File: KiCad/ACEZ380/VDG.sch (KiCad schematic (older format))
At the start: 32 parts, among them Q1 2N3904, Q100 2N3904, X1 CRYSTALHC49U-V 6.556MHz

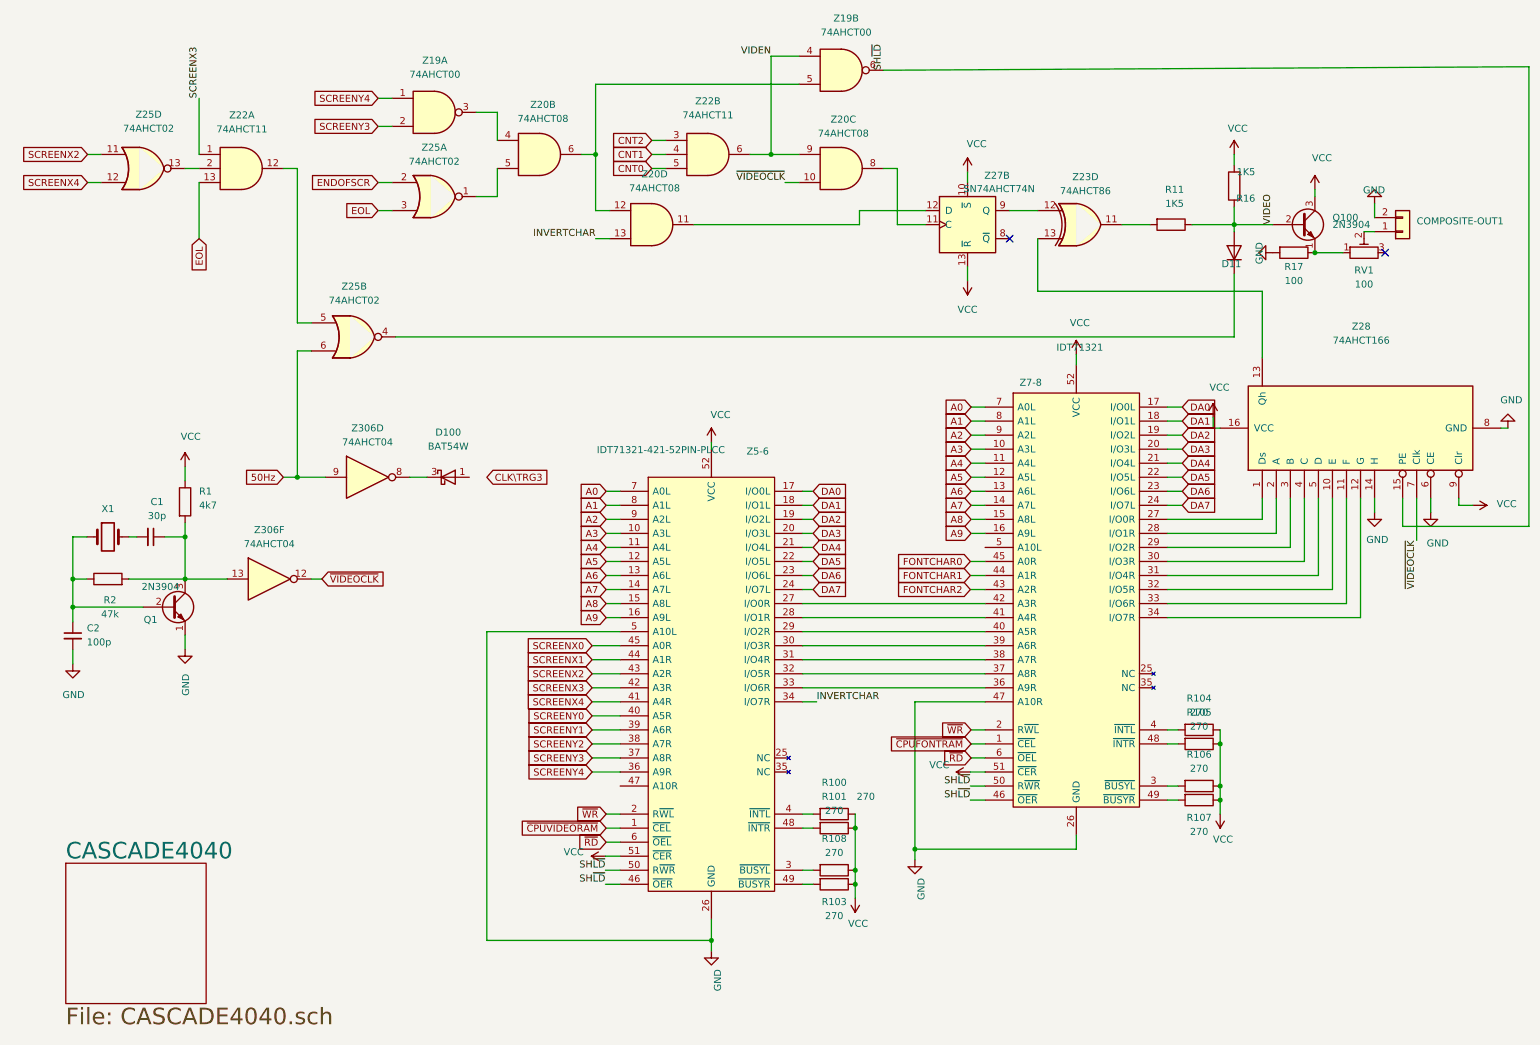
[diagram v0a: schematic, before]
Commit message: Remove SMD.
Standardise Z180 and add Z380.


Signed-off-by: John Bradley <flypie@rocketmail.com>
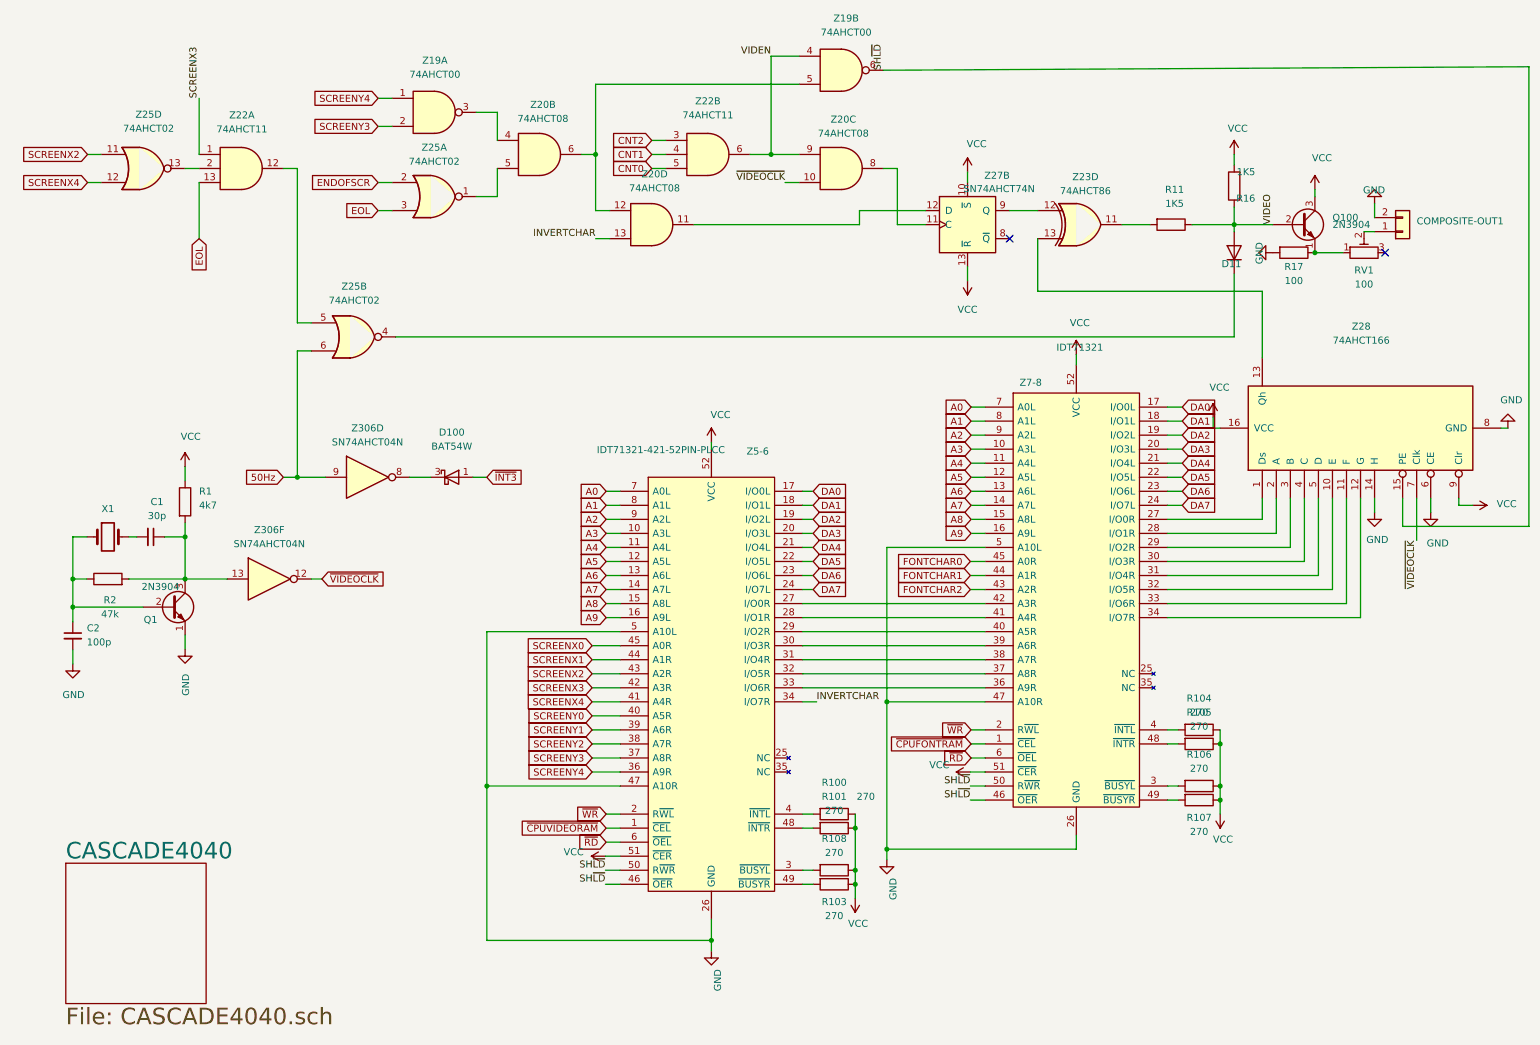
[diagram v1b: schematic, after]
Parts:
- Z306: value 74AHCT04 -> SN74AHCT04N; footprint Package_DIP:DIP-14_W7.62mm_Socket -> Package_DIP:DIP-16_W7.62mm_Socket
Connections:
- net GND: now also Z5-6.47 (A10R), Z7-8.5 (A10L)
- net ~INT3: now reaches D100.1 (A)
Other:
- moved on the sheet: D100
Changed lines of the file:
@@
 $Descr A4 11693 8268
 encoding utf-8
-Sheet 3 9
+Sheet 5 9
 Title "JupiterAceZ180"
 Date "2019-08-26"
@@
 P 2900 3750
 F 0 "Z306" H 2900 4100 50  0000 C CNN
-F 1 "74AHCT04" H 2900 4000 50  0000 C CNN
-F 2 "Package_DIP:DIP-14_W7.62mm_Socket" H 2900 3750 50  0001 C CNN
+F 1 "SN74AHCT04N" H 2900 4000 50  0000 C CNN
+F 2 "Package_DIP:DIP-16_W7.62mm_Socket" H 2900 3750 50  0001 C CNN
 F 3 "https:~/assets.nexperia.com/documents/data-sheet/74HC_AHCT04.pdf" H 2900 3750 50  0001 C CNN
 	4    2900 3750
@@
 Wire Wire Line
 	1600 1550 1700 1550
-Wire Wire Line
-	3200 3750 3325 3750
 Wire Wire Line
 	2400 2850 2500 2850
@@
 L Diode:BAT54W D100
 U 1 1 5E84D6D1
-P 3475 3750
-F 0 "D100" H 3475 4070 50  0000 C CNN
-F 1 "BAT54W" H 3475 3970 50  0000 C CNN
-F 2 "Package_TO_SOT_SMD:SOT-323_SC-70" H 3475 3575 50  0001 C CNN
-F 3 "https:~/assets.nexperia.com/documents/data-sheet/BAT54W_SER.pdf" H 3475 3750 50  0001 C CNN
-	1    3475 3750
+P 3500 3750
+F 0 "D100" H 3500 4070 50  0000 C CNN
+F 1 "BAT54W" H 3500 3970 50  0000 C CNN
+F 2 "Package_TO_SOT_SMD:SOT-323_SC-70" H 3500 3575 50  0001 C CNN
+F 3 "https:~/assets.nexperia.com/documents/data-sheet/BAT54W_SER.pdf" H 3500 3750 50  0001 C CNN
+	1    3500 3750
 	1    0    0    -1
 $EndComp
@@
 P 2200 4475
 F 0 "Z306" H 2200 4825 50  0000 C CNN
-F 1 "74AHCT04" H 2200 4725 50  0000 C CNN
-F 2 "Package_DIP:DIP-14_W7.62mm_Socket" H 2200 4475 50  0001 C CNN
+F 1 "SN74AHCT04N" H 2200 4725 50  0000 C CNN
+F 2 "Package_DIP:DIP-16_W7.62mm_Socket" H 2200 4475 50  0001 C CNN
 F 3 "https://assets.nexperia.com/documents/data-sheet/74AHC_AHCT04.pdf" H 2200 4475 50  0001 C CNN
 	6    2200 4475
@@
 ~VIDEOCLK
 Text GLabel 3750 3750 2    50   Input ~ 0
-CLK\TRG3
+~INT3
 Wire Wire Line
 	6375 6150 6375 6250
@@
 	2400 3750 2600 3750
 Wire Wire Line
-	6800 6400 7950 6400
-Wire Wire Line
-	7300 5350 6800 5350
-Wire Wire Line
-	6800 5350 6800 6400
+	6600 6400 7950 6400
+Wire Wire Line
+	7300 5350 6600 5350
+Wire Wire Line
+	6600 5350 6600 6400
 Wire Wire Line
 	5350 7050 3750 7050
 Wire Wire Line
-	3750 7050 3750 4850
+	3750 7050 3750 5950
 Wire Wire Line
 	3750 4850 4700 4850
@@
 L power:GND #0119
 U 1 1 60749C0A
-P 6800 6475
-F 0 "#0119" H 6800 6225 50  0001 C CNN
-F 1 "GND" V 6845 6345 50  0000 R CNN
-F 2 "" H 6800 6475 50  0001 C CNN
-F 3 "" H 6800 6475 50  0001 C CNN
-	1    6800 6475
-	1    0    0    -1
-$EndComp
-Wire Wire Line
-	6800 6475 6800 6400
-Connection ~ 6800 6400
+P 6600 6475
+F 0 "#0119" H 6600 6225 50  0001 C CNN
+F 1 "GND" V 6645 6345 50  0000 R CNN
+F 2 "" H 6600 6475 50  0001 C CNN
+F 3 "" H 6600 6475 50  0001 C CNN
+	1    6600 6475
+	1    0    0    -1
+$EndComp
+Wire Wire Line
+	6600 6475 6600 6400
+Connection ~ 6600 6400
 $Comp
 L Device:R R100
@@
 	0    1    1    0
 $EndComp
+Wire Wire Line
+	4700 5950 3750 5950
+Connection ~ 3750 5950
+Wire Wire Line
+	3750 5950 3750 4850
+Wire Wire Line
+	7300 4250 6600 4250
+Wire Wire Line
+	6600 4250 6600 5350
+Connection ~ 6600 5350
+Wire Wire Line
+	3750 3750 3650 3750
+Wire Wire Line
+	3200 3750 3350 3750
 $EndSCHEMATC

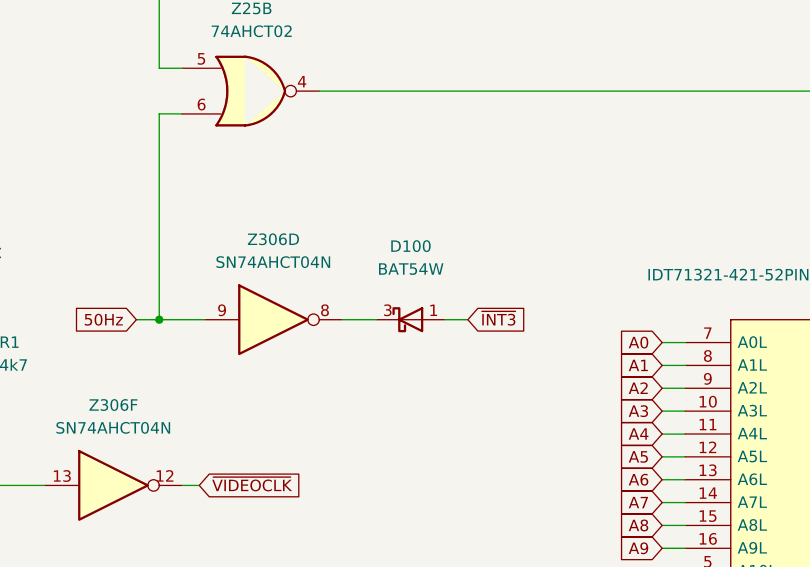
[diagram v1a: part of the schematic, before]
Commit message: Update ACE3NOKB to reflect errors in Mem Decode. ACE5NOKB test SMT ideas. Added 180 & 380.
Signed-off-by: John Bradley <flypie@rocketmail.com>
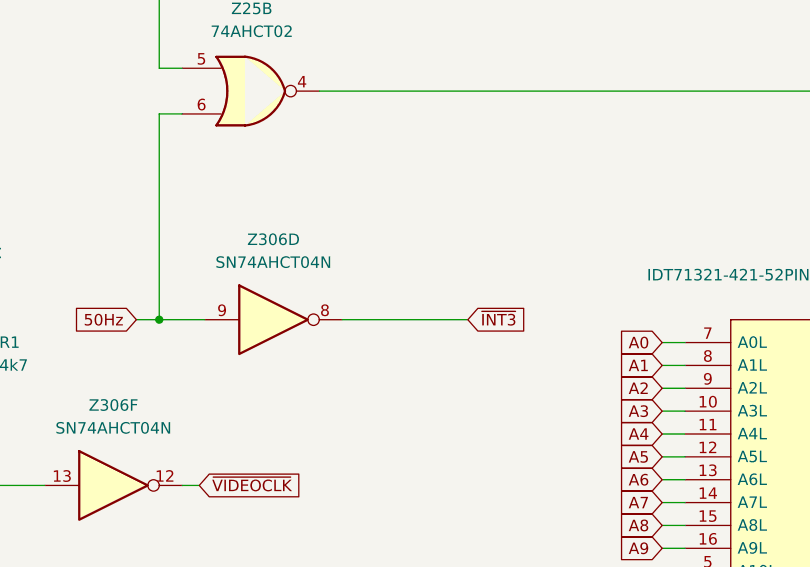
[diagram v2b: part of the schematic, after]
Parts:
- removed D100: BAT54W, Package_TO_SOT_SMD:SOT-323_SC-70, symbol Diode:BAT54W
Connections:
- net ~INT3: now also Z306.8
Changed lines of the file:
@@
 U 2 1 5F80C856
 P 7175 1950
-AR Path="/5F80C856" Ref="Z27"  Part="2"
-AR Path="/5FA4DA0E/5F80C856" Ref="Z27"  Part="2"
-AR Path="/5E2F9A69/5F80C856" Ref="Z27"  Part="2"
-AR Path="/5DAF6158/5F80C856" Ref="Z27"  Part="2"
 F 0 "Z27" H 7385 2300 50  0000 C CNN
 F 1 "SN74AHCT74N" H 7400 2205 50  0000 C CNN
@@
 	1    0    0    -1
 $EndComp
-$Comp
-L Diode:BAT54W D100
-U 1 1 5E84D6D1
-P 3500 3750
-F 0 "D100" H 3500 4070 50  0000 C CNN
-F 1 "BAT54W" H 3500 3970 50  0000 C CNN
-F 2 "Package_TO_SOT_SMD:SOT-323_SC-70" H 3500 3575 50  0001 C CNN
-F 3 "https:~/assets.nexperia.com/documents/data-sheet/BAT54W_SER.pdf" H 3500 3750 50  0001 C CNN
-	1    3500 3750
-	1    0    0    -1
-$EndComp
 Wire Wire Line
 	9075 2300 9075 2750
@@
 U 1 1 5F80C938
 P 7300 3250
-AR Path="/5F80C938" Ref="Z7-8"  Part="1"
-AR Path="/5FA4DA0E/5F80C938" Ref="Z7-8"  Part="1"
-AR Path="/5E2F9A69/5F80C938" Ref="Z7-8"  Part="1"
-AR Path="/5DAF6158/5F80C938" Ref="Z7-8"  Part="1"
 F 0 "Z7-8" H 7625 3425 50  0000 C CNN
 F 1 "IDT71321" H 7975 3675 50  0000 C CNN
@@
 U 1 1 5F80C942
 P 4700 3850
-AR Path="/5F80C942" Ref="Z5-6"  Part="1"
-AR Path="/5FA4DA0E/5F80C942" Ref="Z5-6"  Part="1"
-AR Path="/5E2F9A69/5F80C942" Ref="Z5-6"  Part="1"
-AR Path="/5DAF6158/5F80C942" Ref="Z5-6"  Part="1"
 F 0 "Z5-6" H 5680 4135 50  0000 C CNN
 F 1 "IDT71321-421-52PIN-PLCC" H 4990 4145 50  0000 C CNN
@@
 Connection ~ 6600 5350
 Wire Wire Line
-	3750 3750 3650 3750
-Wire Wire Line
-	3200 3750 3350 3750
+	3200 3750 3750 3750
 $EndSCHEMATC
